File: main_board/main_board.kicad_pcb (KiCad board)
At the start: 4 copper layers, 67 parts, among them J1 CON-SMA-EDGE-S, J2 TSW-104-14-F-S, J3 TSW-104-14-F-S, U1 LT1722CS5-TRMPBF, U12 MIC5365-3.3YC5-TR, U2 TS5A4624DCKR, U3 AD5160, U4 TS5A4624DCKR, U5 AD8031ARTZ-REEL7, U6 LT1722CS5-TRMPBF, U7 LTC2315CTS8-12-PBF, U8 LT1818IS5-TRMPBF, U9 AP63205WU-7

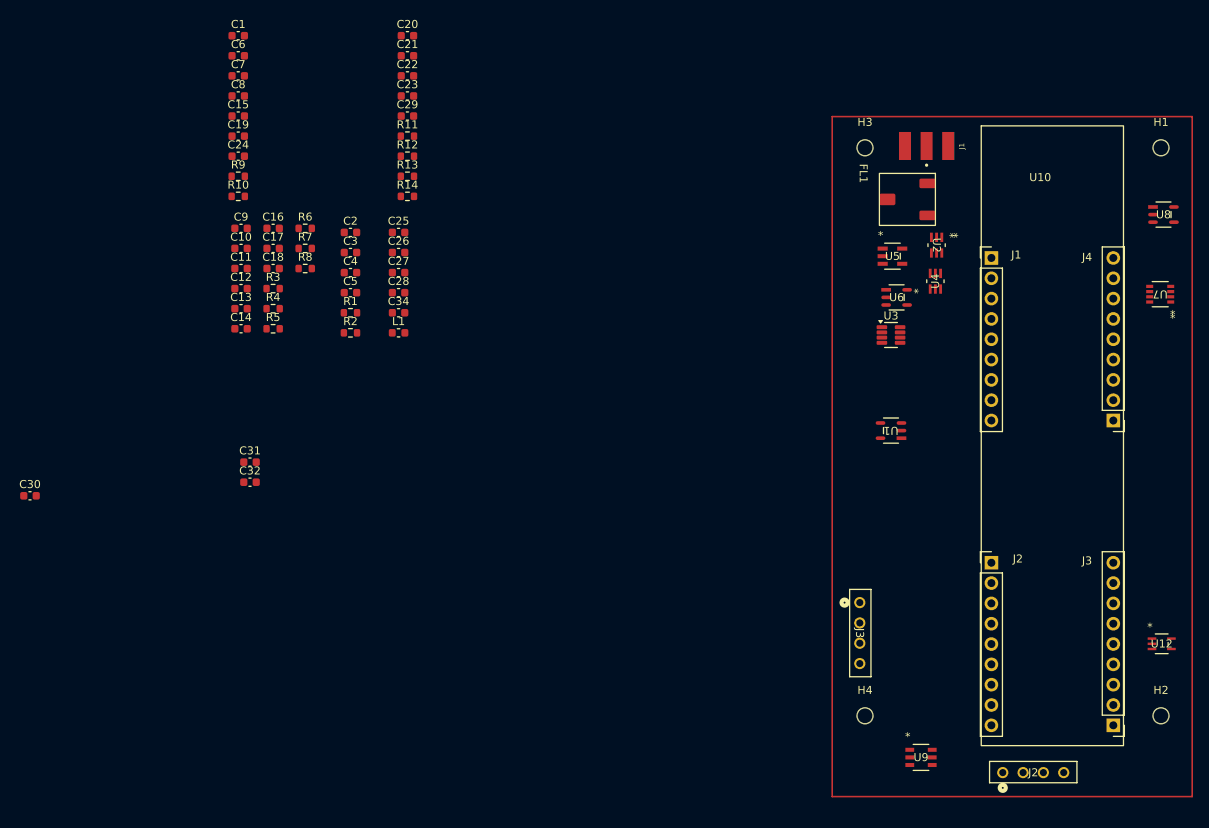
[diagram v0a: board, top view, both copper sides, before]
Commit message: Layout hase been floorplaned, needs routing.
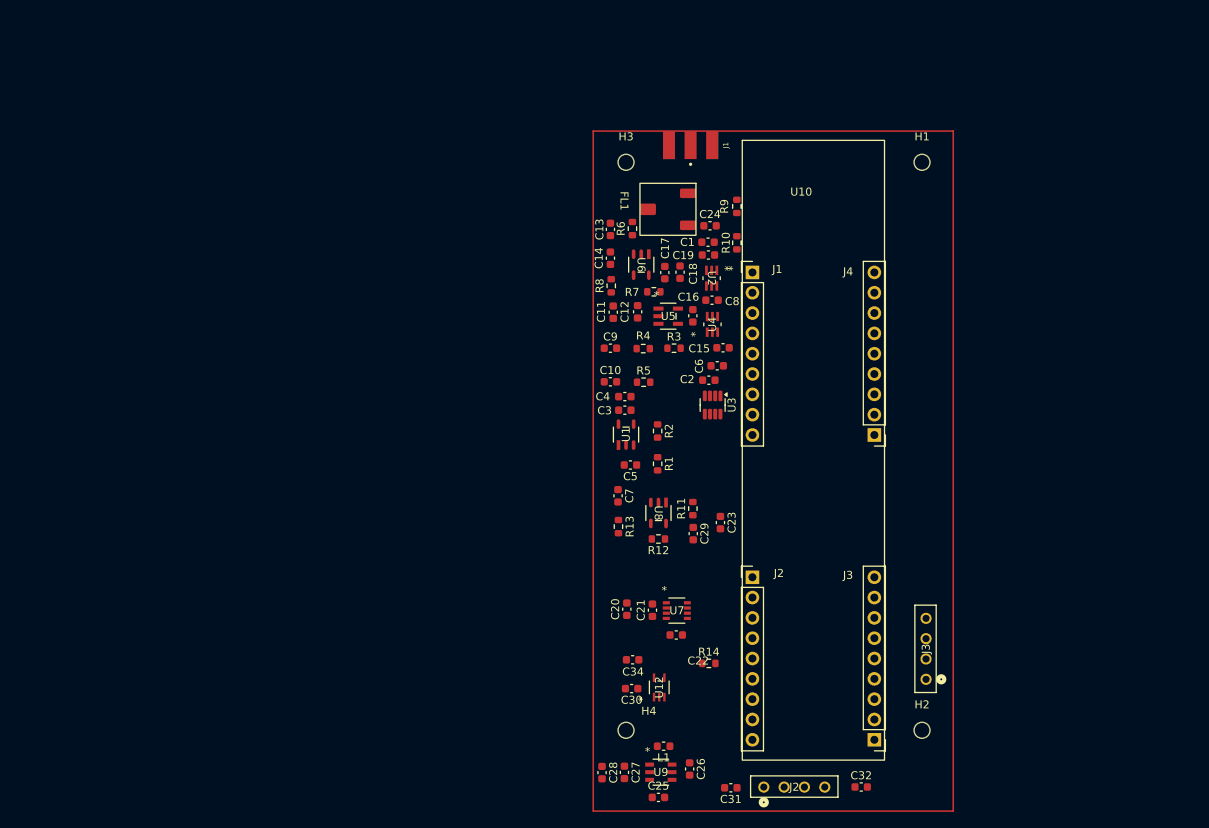
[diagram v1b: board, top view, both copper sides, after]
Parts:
- moved C32 85.4 mm to (151.6, 149.3)
- moved C30 79.0 mm to (122.9, 137.0), turned to 180 degrees
- moved C25 77.7 mm to (126.3, 150.6)
- moved C22 77.5 mm to (128.5, 130.3), turned to 180 degrees
- moved C20 76.8 mm to (122.3, 127.1), turned to 90 degrees
- moved C21 75.8 mm to (125.5, 127.2), turned to 90 degrees
- moved C26 74.1 mm to (130.2, 147.1), turned to -90 degrees
- moved U8 73.3 mm to (126.3, 115.1), turned to -90 degrees
- moved C31 72.6 mm to (135.3, 149.4), turned to 180 degrees
- moved U7 72.2 mm to (128.6, 127.3), turned to 0 degrees
- moved C6 71.3 mm to (133.6, 96.7)
- moved C7 70.8 mm to (121.2, 112.9), turned to -90 degrees
- moved R14 69.5 mm to (132.6, 133.9)
- moved C27 68.6 mm to (122.0, 147.5), turned to -90 degrees
- moved C15 67.2 mm to (134.4, 94.4)
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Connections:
- U10 pad 1: /Bypass_ctrl -> unconnected-(U10-Pad1)
- U10 pad 16: unconnected-(U10-Pad16) -> /CS_bar
- U10 pad 18: unconnected-(U10-Pad18) -> /SCK
- U10 pad 19: /uart -> unconnected-(U10-Pad19)
- U10 pad 2: /Pot_CLK -> unconnected-(U10-Pad2)
- U10 pad 21: unconnected-(U10-Pad21) -> /Serial_Data_Out
- U10 pad 29: unconnected-(U10-Pad29) -> /uart
- U10 pad 3: /Pot_CS -> unconnected-(U10-Pad3)
- U10 pad 42: unconnected-(U10-Pad42) -> /Pot_SDI
- U10 pad 44: /CS_bar -> /Pot_CS
- U10 pad 45: /SCK -> unconnected-(U10-Pad45)
- U10 pad 46: unconnected-(U10-Pad46) -> /Pot_CLK
- U10 pad 48: /Serial_Data_Out -> /Bypass_ctrl
- U10 pad 6: /Pot_SDI -> unconnected-(U10-Pad6)

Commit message: finished board, waiting for approval.
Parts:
- added G***: LOGO, Graphics:grapphics, F.Cu at (158.7, 148.6)
- moved R14 2.07 mm to (134.6, 133.4)
- moved R9 0.94 mm to (136.0, 75.8)
- moved U2 0.78 mm to (133.7, 85.8), turned to 90 degrees
- moved C16 0.58 mm to (130.0, 90.4)
- moved U1 0.53 mm to (121.7, 105.3)
- moved U5 0.53 mm to (127.0, 90.4)
- moved C7 0.48 mm to (120.8, 112.9)
- moved R13 0.48 mm to (120.8, 116.8)
- moved C24 0.47 mm to (133.2, 79.2)
- moved FL1 0.43 mm to (124.4, 73.8)
- moved C28 0.41 mm to (119.3, 147.1)
- moved R8 0.40 mm to (120.6, 87.0)
- moved C27 0.38 mm to (122.1, 147.1)
- moved C4 0.38 mm to (121.7, 100.5)
- moved C3 0.38 mm to (121.7, 102.2)
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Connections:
- U10 pad 20: unconnected-(U10-Pad20) -> /Serial_Data_Out
- U10 pad 21: /Serial_Data_Out -> unconnected-(U10-Pad21)
- U2 pad 1: /Filter_out -> /Bypass_ctrl
- U2 pad 5: /Bypass -> /Filter_out
- U4 pad 1: /PGA_in -> /Bypass_ctrl
- U4 pad 5: /Bypass -> /PGA_in
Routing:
- net GND: track 0.00 -> 102.1 mm, vias 0 -> 21
- net +5V: track 0.00 -> 68.3 mm, vias 0 -> 13
- net /Bypass_ctrl: track 0.00 -> 32.0 mm, vias 0 -> 2
- net /Pot_SDI: track 0.00 -> 27.9 mm, vias 0 -> 1
- net /Pot_CLK: track 0.00 -> 27.8 mm, vias 0 -> 1
- net /Pot_CS: track 0.00 -> 26.5 mm, vias 0 -> 1
- net /High Gain Amplifier/Vref: track 0.00 -> 23.1 mm
- net /HGA_out: track 0.00 -> 21.3 mm
- net /PGA/Vout: track 0.00 -> 20.9 mm
- net Net-(U7-AIN): track 0.00 -> 20.0 mm
- net +9V: track 0.00 -> 18.9 mm
- net Net-(U5-+IN): track 0.00 -> 16.9 mm
- net Net-(C13-Pad2): track 0.00 -> 14.7 mm, vias 0 -> 2
- net Net-(U6--IN): track 0.00 -> 14.2 mm
- net /SCK: track 0.00 -> 14.0 mm, vias 0 -> 1
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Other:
- board outline added: 45 x 85 mm
- board text added: "AVY DAWGS"

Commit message: Final PCB design, waiting for group approval.
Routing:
- added copper zone on B.Cu, net GND
- added copper zone on F.Cu, net GND
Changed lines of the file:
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@@
 	)
 	(gr_rect
-		(start 118.13 67.32)
-		(end 163.13 152.32)
+		(start 118.13 67.3)
+		(end 163.13 152.3)
 		(stroke
 			(width 0.2)
@@
 	)
 	(segment
-		(start 135.425 133.4)
+		(start 136.4 133.25)
 		(end 135.575 133.25)
 		(width 0.2032)
@@
 	)
 	(via
-		(at 135.425 133.4)
+		(at 136.4 133.25)
 		(size 0.61)
 		(drill 0.3)
@@
 	)
 	(segment
-		(start 135.575 133.25)
+		(start 136.4 133.25)
 		(end 138.03 133.25)
 		(width 0.2032)
@@
 	)
 	(segment
+		(start 133.775 132.1)
+		(end 133.775 133.4)
+		(width 0.2032)
+		(layer "F.Cu")
+		(net 55)
+	)
+	(segment
 		(start 129.89445 127.585001)
 		(end 130.585001 127.585001)
@@
 	)
 	(via
-		(at 133.775 133.4)
+		(at 133.775 132.1)
 		(size 0.61)
 		(drill 0.3)
@@
 	)
 	(segment
-		(start 133.775 130.775)
-		(end 131 128)
+		(start 133.775 132.1)
+		(end 133.775 130.775)
 		(width 0.2032)
 		(layer "B.Cu")
@@
 	)
 	(segment
-		(start 133.775 133.4)
-		(end 133.775 130.775)
+		(start 133.775 130.775)
+		(end 131 128)
 		(width 0.2032)
 		(layer "B.Cu")
@@
 		(net 2)
 		(net_name "GND")
+		(layer "F.Cu")
+		(hatch edge 0.5)
+		(priority 2)
+		(connect_pads
+			(clearance 0.5)
+		)
+		(min_thickness 0.25)
+		(filled_areas_thickness no)
+		(fill yes
+			(thermal_gap 0.5)
+			(thermal_bridge_width 0.5)
+		)
+		(polygon
+			(pts
+				(xy 118.8 68) (xy 118.5 151.9) (xy 162.4 151.7) (xy 162.4 68)
+			)
+		)
+	)
+	(zone
+		(net 2)
+		(net_name "GND")
+		(layer "B.Cu")
+		(hatch edge 0.5)
+		(priority 3)
+		(connect_pads
+			(clearance 0.5)
+		)
+		(min_thickness 0.25)
+		(filled_areas_thickness no)
+		(fill yes
+			(thermal_gap 0.5)
+			(thermal_bridge_width 0.5)
+		)
+		(polygon
+			(pts
+				(xy 118.5 151.9) (xy 162.4 151.7) (xy 162.4 68) (xy 118.8 68)
+			)
+		)
+	)
+	(zone
+		(net 2)
+		(net_name "GND")
 		(layer "In1.Cu")
 		(hatch edge 0.5)
@@
 		(polygon
 			(pts
-				(xy 118.13 67.32) (xy 118.13 152.32) (xy 163.13 152.32) (xy 163.13 67.32)
+				(xy 118.8 68) (xy 118.5 151.9) (xy 162.4 151.7) (xy 162.4 68)
 			)
 		)
@@
 		(polygon
 			(pts
-				(xy 118.13 67.32) (xy 118.13 152.27) (xy 163.13 152.32) (xy 163.13 67.32)
+				(xy 118.8 68) (xy 118.5 151.9) (xy 162.4 151.7) (xy 162.4 68)
 			)
 		)
